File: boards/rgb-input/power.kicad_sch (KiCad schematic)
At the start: 20 parts, among them U3 R-78K5.0-1.0

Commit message: input board shaping up to be lit.
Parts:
- renumbered D18 to D26
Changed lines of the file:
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@@
   (symbol (lib_id "Device:D_Schottky") (at 189.23 88.9 270) (unit 1)
     (in_bom yes) (on_board yes) (dnp no) (fields_autoplaced)
-    (property "Reference" "D18" (at 192.405 87.3125 90)
+    (property "Reference" "D26" (at 192.405 87.3125 90)
       (effects (font (size 1.27 1.27)) (justify left))
     )
@@
   (symbol (lib_id "Device:D_Schottky") (at 242.57 80.01 180) (unit 1)
     (in_bom yes) (on_board yes) (dnp no) (fields_autoplaced)
-    (property "Reference" "D18" (at 242.57 73.66 0)
+    (property "Reference" "D26" (at 242.57 73.66 0)
       (effects (font (size 1.27 1.27)))
     )
@@
   (symbol (lib_id "Device:D_Schottky") (at 95.25 80.01 180) (unit 1)
     (in_bom yes) (on_board yes) (dnp no) (fields_autoplaced)
-    (property "Reference" "D18" (at 95.25 73.66 0)
-      (effects (font (size 1.27 1.27)))
-    )
+    (property "Reference" "D26" (at 95.25 73.66 0)
+      (effects (font (size 1.27 1.27)))
+    )

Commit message: more layout checks on the input board
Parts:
- added J1: Barrel_Jack, Connector_BarrelJack:BarrelJack_CUI_PJ-063AH_Horizontal, symbol Connector:Barrel_Jack
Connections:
- net +24V: now also J1.1
- net GNDD: now also J1.2
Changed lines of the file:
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@@
   (junction (at 166.37 80.01) (diameter 0) (color 0 0 0 0)
   )
+  (junction (at 31.75 80.01) (diameter 0) (color 0 0 0 0)
+  )
   (junction (at 69.85 80.01) (diameter 0) (color 0 0 0 0)
   )
@@
   (junction (at 123.19 96.52) (diameter 0) (color 0 0 0 0)
   )
+  (junction (at 69.85 96.52) (diameter 0) (color 0 0 0 0)
+  )
   (junction (at 215.9 96.52) (diameter 0) (color 0 0 0 0)
   )
@@
     (stroke (width 0) (type default))
   )
+  (wire (pts (xy 31.75 87.63) (xy 30.48 87.63))
+    (stroke (width 0) (type default))
+  )
   (wire (pts (xy 69.85 90.17) (xy 69.85 96.52))
     (stroke (width 0) (type default))
@@
     (stroke (width 0) (type default))
   )
+  (wire (pts (xy 31.75 96.52) (xy 31.75 92.71))
+    (stroke (width 0) (type default))
+  )
   (wire (pts (xy 35.56 80.01) (xy 44.45 80.01))
     (stroke (width 0) (type default))
@@
     (stroke (width 0) (type default))
   )
+  (wire (pts (xy 31.75 80.01) (xy 31.75 87.63))
+    (stroke (width 0) (type default))
+  )
   (wire (pts (xy 116.84 80.01) (xy 123.19 80.01))
     (stroke (width 0) (type default))
@@
     (stroke (width 0) (type default))
   )
+  (wire (pts (xy 69.85 96.52) (xy 31.75 96.52))
+    (stroke (width 0) (type default))
+  )
   (wire (pts (xy 166.37 80.01) (xy 170.18 80.01))
+    (stroke (width 0) (type default))
+  )
+  (wire (pts (xy 31.75 92.71) (xy 30.48 92.71))
     (stroke (width 0) (type default))
   )
@@
         )
       )
+    )
+  )
+  (symbol (lib_id "Connector:Barrel_Jack") (at 22.86 90.17 0) (unit 1)
+    (in_bom yes) (on_board yes) (dnp no) (fields_autoplaced)
+    (property "Reference" "J1" (at 22.86 81.28 0)
+      (effects (font (size 1.27 1.27)))
+    )
+    (property "Value" "Barrel_Jack" (at 22.86 83.82 0)
+      (effects (font (size 1.27 1.27)))
+    )
+    (property "Footprint" "Connector_BarrelJack:BarrelJack_CUI_PJ-063AH_Horizontal" (at 24.13 91.186 0)
+      (effects (font (size 1.27 1.27)) hide)
+    )
+    (property "Datasheet" "~" (at 24.13 91.186 0)
+      (effects (font (size 1.27 1.27)) hide)
+    )
+    (pin "1")
+    (pin "2")
+    (instances
+      (project "rgb-input"
+        (path "/c83c6236-96e9-46ad-9d7a-9e2efa4a7966/e112a34f-fd2f-43cb-bf5d-a7f5e57b6bef"
+          (reference "J1") (unit 1)
+        )
+      )

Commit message: so much routing.
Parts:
- removed R37: 0R, Resistor_SMD:R_0805_2012Metric_Pad1.20x1.40mm_HandSolder, symbol Device:R_Small_US
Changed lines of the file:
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@@
   (junction (at 231.14 80.01) (diameter 0) (color 0 0 0 0)
   )
-  (junction (at 156.21 111.76) (diameter 0) (color 0 0 0 0)
-  )
   (junction (at 189.23 96.52) (diameter 0) (color 0 0 0 0)
   )
@@
     (stroke (width 0) (type default))
   )
-  (wire (pts (xy 168.91 111.76) (xy 177.8 111.76))
-    (stroke (width 0) (type default))
-  )
   (wire (pts (xy 69.85 96.52) (xy 31.75 96.52))
     (stroke (width 0) (type default))
@@
     (stroke (width 0) (type default))
   )
-  (wire (pts (xy 156.21 111.76) (xy 156.21 113.03))
-    (stroke (width 0) (type default))
-  )
   (wire (pts (xy 104.14 85.09) (xy 104.14 80.01))
-    (stroke (width 0) (type default))
-  )
-  (wire (pts (xy 156.21 111.76) (xy 163.83 111.76))
     (stroke (width 0) (type default))
   )
@@
     )
   )
-  (symbol (lib_id "Device:R_Small_US") (at 166.37 111.76 270) (unit 1)
-    (in_bom yes) (on_board yes) (dnp no) (fields_autoplaced)
-    (property "Reference" "R37" (at 166.37 105.41 90)
-      (effects (font (size 1.27 1.27)))
-    )
-    (property "Value" "0R" (at 166.37 107.95 90)
-      (effects (font (size 1.27 1.27)))
-    )
-    (property "Footprint" "Resistor_SMD:R_0805_2012Metric_Pad1.20x1.40mm_HandSolder" (at 166.37 111.76 0)
-      (effects (font (size 1.27 1.27)) hide)
-    )
-    (property "Datasheet" "~" (at 166.37 111.76 0)
-      (effects (font (size 1.27 1.27)) hide)
-    )
-    (property "Vendor" " 652-CR0805JW-102ELF " (at 166.37 111.76 0)
-      (effects (font (size 1.27 1.27)) hide)
-    )
-    (pin "1")
-    (pin "2")
-    (instances
-      (project "rgb-input"
-        (path "/c83c6236-96e9-46ad-9d7a-9e2efa4a7966"
-          (reference "R37") (unit 1)
-        )
-        (path "/c83c6236-96e9-46ad-9d7a-9e2efa4a7966/e112a34f-fd2f-43cb-bf5d-a7f5e57b6bef"
-          (reference "R37") (unit 1)
-        )
-      )
-    )
-  )
   (symbol (lib_id "Device:D_Schottky") (at 242.57 80.01 180) (unit 1)
     (in_bom yes) (on_board yes) (dnp no) (fields_autoplaced)
@@
         (path "/c83c6236-96e9-46ad-9d7a-9e2efa4a7966/e112a34f-fd2f-43cb-bf5d-a7f5e57b6bef"
           (reference "C47") (unit 1)
-        )
-      )
-    )
-  )
-  (symbol (lib_id "power:PWR_FLAG") (at 156.21 111.76 0) (unit 1)
-    (in_bom yes) (on_board yes) (dnp no) (fields_autoplaced)
-    (property "Reference" "#FLG03" (at 156.21 109.855 0)
-      (effects (font (size 1.27 1.27)) hide)
-    )
-    (property "Value" "PWR_FLAG" (at 156.21 106.68 0)
-      (effects (font (size 1.27 1.27)))
-    )
-    (property "Footprint" "" (at 156.21 111.76 0)
-      (effects (font (size 1.27 1.27)) hide)
-    )
-    (property "Datasheet" "~" (at 156.21 111.76 0)
-      (effects (font (size 1.27 1.27)) hide)
-    )
-    (pin "1")
-    (instances
-      (project "rgb-input"
-        (path "/c83c6236-96e9-46ad-9d7a-9e2efa4a7966/e112a34f-fd2f-43cb-bf5d-a7f5e57b6bef"
-          (reference "#FLG03") (unit 1)
         )
       )
@@
         )
       )
-    )
-  )
-  (symbol (lib_id "power:GNDPWR") (at 156.21 113.03 0) (unit 1)
-    (in_bom yes) (on_board yes) (dnp no) (fields_autoplaced)
-    (property "Reference" "#PWR056" (at 156.21 118.11 0)
-      (effects (font (size 1.27 1.27)) hide)
-    )
-    (property "Value" "GNDPWR" (at 156.083 116.84 0)
-      (effects (font (size 1.27 1.27)))
-    )
-    (property "Footprint" "" (at 156.21 114.3 0)
-      (effects (font (size 1.27 1.27)) hide)
-    )
-    (property "Datasheet" "" (at 156.21 114.3 0)
-      (effects (font (size 1.27 1.27)) hide)
-    )
-    (pin "1")
-    (instances
-      (project "rgb-input"
-        (path "/c83c6236-96e9-46ad-9d7a-9e2efa4a7966"
-          (reference "#PWR056") (unit 1)
-        )
-        (path "/c83c6236-96e9-46ad-9d7a-9e2efa4a7966/e112a34f-fd2f-43cb-bf5d-a7f5e57b6bef"
-          (reference "#PWR09") (unit 1)
-        )
-      )

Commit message: too much routing
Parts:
- removed C1: 22nF, Capacitor_SMD:C_0805_2012Metric_Pad1.18x1.45mm_HandSolder, symbol Device:C_Small
- removed C27: 1nF, Capacitor_SMD:C_0805_2012Metric_Pad1.18x1.45mm_HandSolder, symbol Device:C_Small
- removed U3: R-78K5.0-1.0, gnarboard:RECOM R-78K, symbol Regulator_Switching:R-78B3.3-2.0
- added U3: XL1509-5.0, Package_SO:SOIC-8_3.9x4.9mm_P1.27mm, symbol Regulator_Switching:XL1509-5.0
- C1: value 47uF/6.3v -> 100uF/10v; footprint Capacitor_SMD:C_0805_2012Metric_Pad1.18x1.45mm_HandSolder -> Capacitor_Tantalum_SMD:CP_EIA-3528-21_Kemet-B; symbol Device:C_Small -> Device:C_Polarized_Small_US; Vendor 08053C104KAT4A -> TAJC107K010RNJ
- L2: value SMMS0650-470M -> SMMS0650-680M
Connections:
- net +5V: now also U3.3 (FB)
- net GNDD: now also U3.4 (~{EN}), U3.5 (GND), U3.6 (GND), U3.7 (GND), U3.8 (GND)
- net at C1.1, C1.1, C1.1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: now also U3.1 (VIN)
- net at D26.1 (K), L2.1: now also U3.2 (OUT)
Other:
- moved on the sheet: C1, D26, R38

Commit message: various cleanups and tidying
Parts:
- J1: symbol Connector:Barrel_Jack -> Connector:Barrel_Jack_MountingPin
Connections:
- net GNDD: now also J1.MP (MountPin)
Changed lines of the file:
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@@
   (junction (at 173.99 111.76) (diameter 0) (color 0 0 0 0)
   )
+  (junction (at 31.75 97.79) (diameter 0) (color 0 0 0 0)
+  )
   (junction (at 31.75 80.01) (diameter 0) (color 0 0 0 0)
   )
   (junction (at 69.85 80.01) (diameter 0) (color 0 0 0 0)
   )
-  (junction (at 173.99 96.52) (diameter 0) (color 0 0 0 0)
+  (junction (at 173.99 97.79) (diameter 0) (color 0 0 0 0)
   )
   (junction (at 209.55 80.01) (diameter 0) (color 0 0 0 0)
@@
   (junction (at 231.14 80.01) (diameter 0) (color 0 0 0 0)
   )
-  (junction (at 189.23 96.52) (diameter 0) (color 0 0 0 0)
-  )
-  (junction (at 123.19 96.52) (diameter 0) (color 0 0 0 0)
-  )
-  (junction (at 163.83 96.52) (diameter 0) (color 0 0 0 0)
-  )
-  (junction (at 69.85 96.52) (diameter 0) (color 0 0 0 0)
+  (junction (at 189.23 97.79) (diameter 0) (color 0 0 0 0)
+  )
+  (junction (at 123.19 97.79) (diameter 0) (color 0 0 0 0)
+  )
+  (junction (at 163.83 97.79) (diameter 0) (color 0 0 0 0)
+  )
+  (junction (at 69.85 97.79) (diameter 0) (color 0 0 0 0)
   )
   (junction (at 86.36 80.01) (diameter 0) (color 0 0 0 0)
   )
-  (junction (at 153.67 96.52) (diameter 0) (color 0 0 0 0)
+  (junction (at 153.67 97.79) (diameter 0) (color 0 0 0 0)
   )
   (junction (at 35.56 80.01) (diameter 0) (color 0 0 0 0)
@@
   (junction (at 153.67 80.01) (diameter 0) (color 0 0 0 0)
   )
-  (junction (at 104.14 96.52) (diameter 0) (color 0 0 0 0)
+  (junction (at 104.14 97.79) (diameter 0) (color 0 0 0 0)
   )
   (junction (at 252.73 80.01) (diameter 0) (color 0 0 0 0)
@@
   (junction (at 77.47 80.01) (diameter 0) (color 0 0 0 0)
   )
-  (junction (at 138.43 96.52) (diameter 0) (color 0 0 0 0)
+  (junction (at 138.43 97.79) (diameter 0) (color 0 0 0 0)
   )
   (junction (at 147.32 80.01) (diameter 0) (color 0 0 0 0)
   )
-  (junction (at 86.36 96.52) (diameter 0) (color 0 0 0 0)
-  )
-  (wire (pts (xy 138.43 96.52) (xy 153.67 96.52))
-    (stroke (width 0) (type default))
-  )
-  (wire (pts (xy 138.43 93.98) (xy 138.43 96.52))
+  (junction (at 86.36 97.79) (diameter 0) (color 0 0 0 0)
+  )
+  (wire (pts (xy 138.43 97.79) (xy 153.67 97.79))
+    (stroke (width 0) (type default))
+  )
+  (wire (pts (xy 138.43 93.98) (xy 138.43 97.79))
     (stroke (width 0) (type default))
   )
@@
     (stroke (width 0) (type default))
   )
-  (wire (pts (xy 69.85 90.17) (xy 69.85 96.52))
+  (wire (pts (xy 69.85 90.17) (xy 69.85 97.79))
     (stroke (width 0) (type default))
   )
@@
     (stroke (width 0) (type default))
   )
-  (wire (pts (xy 123.19 96.52) (xy 138.43 96.52))
+  (wire (pts (xy 123.19 97.79) (xy 138.43 97.79))
+    (stroke (width 0) (type default))
+  )
+  (wire (pts (xy 22.86 97.79) (xy 31.75 97.79))
     (stroke (width 0) (type default))
   )
@@
     (stroke (width 0) (type default))
   )
-  (wire (pts (xy 31.75 96.52) (xy 31.75 92.71))
-    (stroke (width 0) (type default))
-  )
-  (wire (pts (xy 173.99 96.52) (xy 189.23 96.52))
+  (wire (pts (xy 31.75 97.79) (xy 31.75 92.71))
+    (stroke (width 0) (type default))
+  )
+  (wire (pts (xy 173.99 97.79) (xy 189.23 97.79))
     (stroke (width 0) (type default))
   )
@@
     (stroke (width 0) (type default))
   )
-  (wire (pts (xy 153.67 96.52) (xy 163.83 96.52))
-    (stroke (width 0) (type default))
-  )
-  (wire (pts (xy 163.83 85.09) (xy 163.83 96.52))
+  (wire (pts (xy 153.67 97.79) (xy 163.83 97.79))
+    (stroke (width 0) (type default))
+  )
+  (wire (pts (xy 163.83 85.09) (xy 163.83 97.79))
     (stroke (width 0) (type default))
   )
@@
     (stroke (width 0) (type default))
   )
-  (wire (pts (xy 153.67 90.17) (xy 153.67 96.52))
+  (wire (pts (xy 153.67 90.17) (xy 153.67 97.79))
     (stroke (width 0) (type default))
   )
@@
     (stroke (width 0) (type default))
   )
-  (wire (pts (xy 163.83 96.52) (xy 173.99 96.52))
-    (stroke (width 0) (type default))
-  )
-  (wire (pts (xy 86.36 91.44) (xy 86.36 96.52))
+  (wire (pts (xy 163.83 97.79) (xy 173.99 97.79))
+    (stroke (width 0) (type default))
+  )
+  (wire (pts (xy 86.36 91.44) (xy 86.36 97.79))
     (stroke (width 0) (type default))
   )
@@
     (stroke (width 0) (type default))
   )
-  (wire (pts (xy 69.85 96.52) (xy 31.75 96.52))
+  (wire (pts (xy 69.85 97.79) (xy 31.75 97.79))
     (stroke (width 0) (type default))
   )
@@
     (stroke (width 0) (type default))
   )
-  (wire (pts (xy 69.85 96.52) (xy 86.36 96.52))
+  (wire (pts (xy 69.85 97.79) (xy 86.36 97.79))
     (stroke (width 0) (type default))
   )
@@
     (stroke (width 0) (type default))
   )
-  (wire (pts (xy 173.99 96.52) (xy 173.99 111.76))
+  (wire (pts (xy 173.99 97.79) (xy 173.99 111.76))
     (stroke (width 0) (type default))
   )
@@
     (stroke (width 0) (type default))
   )
-  (wire (pts (xy 189.23 96.52) (xy 231.14 96.52))
+  (wire (pts (xy 189.23 97.79) (xy 231.14 97.79))
     (stroke (width 0) (type default))
   )
@@
     (stroke (width 0) (type default))
   )
-  (wire (pts (xy 189.23 95.25) (xy 189.23 96.52))
+  (wire (pts (xy 189.23 95.25) (xy 189.23 97.79))
     (stroke (width 0) (type default))
   )
@@
     (stroke (width 0) (type default))
   )
-  (wire (pts (xy 104.14 96.52) (xy 123.19 96.52))
-    (stroke (width 0) (type default))
-  )
-  (wire (pts (xy 123.19 90.17) (xy 123.19 96.52))
+  (wire (pts (xy 104.14 97.79) (xy 123.19 97.79))
+    (stroke (width 0) (type default))
+  )
+  (wire (pts (xy 123.19 90.17) (xy 123.19 97.79))
     (stroke (width 0) (type default))
   )
@@
     (stroke (width 0) (type default))
   )
-  (wire (pts (xy 86.36 96.52) (xy 104.14 96.52))
-    (stroke (width 0) (type default))
-  )
-  (wire (pts (xy 231.14 90.17) (xy 231.14 96.52))
+  (wire (pts (xy 86.36 97.79) (xy 104.14 97.79))
+    (stroke (width 0) (type default))
+  )
+  (wire (pts (xy 231.14 90.17) (xy 231.14 97.79))
     (stroke (width 0) (type default))
   )
@@
     (stroke (width 0) (type default))
   )
-  (wire (pts (xy 104.14 90.17) (xy 104.14 96.52))
+  (wire (pts (xy 104.14 90.17) (xy 104.14 97.79))
     (stroke (width 0) (type default))
   )
@@
     (stroke (width 0) (type default))
   )
-  (wire (pts (xy 173.99 90.17) (xy 173.99 96.52))
+  (wire (pts (xy 173.99 90.17) (xy 173.99 97.79))
     (stroke (width 0) (type default))
   )
@@
     )
   )
-  (symbol (lib_id "Connector:Barrel_Jack") (at 22.86 90.17 0) (unit 1)
+  (symbol (lib_id "Connector:Barrel_Jack_MountingPin") (at 22.86 90.17 0) (unit 1)
     (in_bom yes) (on_board yes) (dnp no) (fields_autoplaced)
     (property "Reference" "J1" (at 22.86 81.28 0)
@@
     (pin "1")
     (pin "2")
-    (instances
-      (project "rgb-input"
+    (pin "MP")
+    (instances
+      (project "rgb-input"

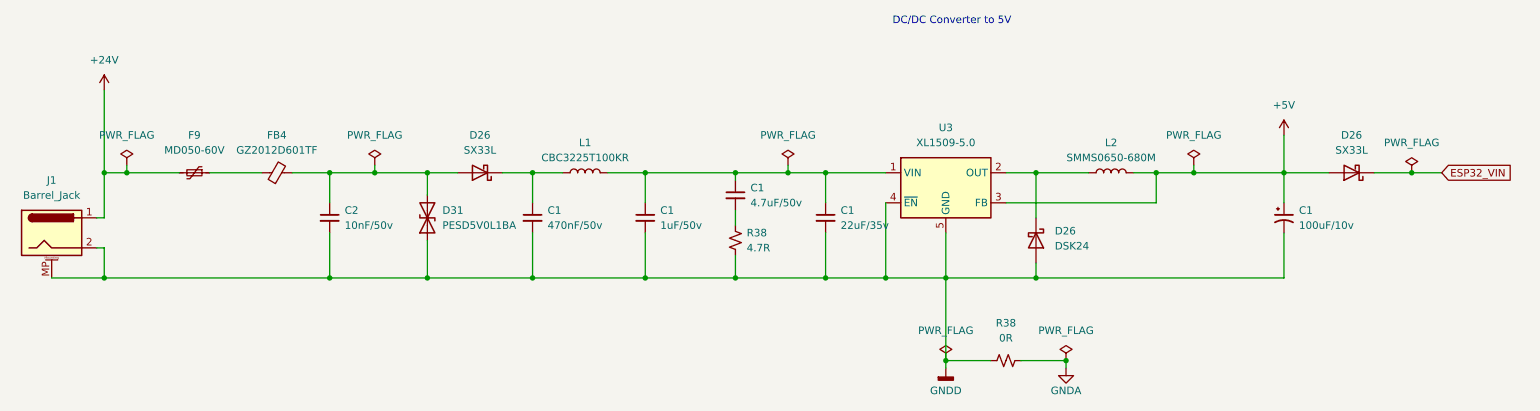
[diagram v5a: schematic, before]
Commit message: added 5v fuse to schematic
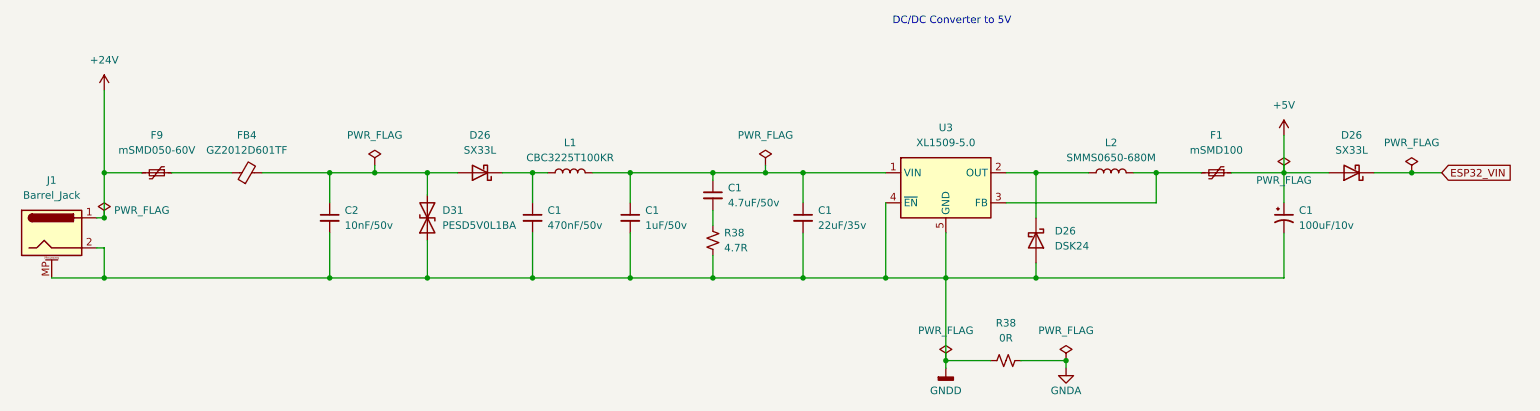
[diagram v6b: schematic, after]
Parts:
- added F1: mSMD100, Fuse:Fuse_1812_4532Metric_Pad1.30x3.40mm_HandSolder, symbol Device:Polyfuse_Small
- F9: value MD050-60V -> mSMD050-60V
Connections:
- net +5V: now also F1.1; no longer L2.2, U3.3 (FB)
- new net: F1.2, L2.2, U3.3 (FB)
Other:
- moved on the sheet: C1, F9, FB4, L1, R38
